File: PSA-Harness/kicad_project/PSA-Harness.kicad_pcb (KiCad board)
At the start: 4 copper layers, 58.3 x 52.5 mm, 20 parts, among them J1 to_EPS_1, J10 B2B_1, J11 B2B_2, J2 to_EPS_2, J3 to_ESP_3, J4 to_car_1, J5 to_car_2, J6 to_car_3, J7 USB_C_Receptacle, J8 B2B_1, J9 B2B_2, U1 DG419LEUA, U2 DG419LEUA

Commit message: cable-board setup
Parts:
- removed J10, J8: B2B_1, Connector_PinHeader_1.27mm:PinHeader_2x15_P1.27mm_Vertical
- removed J11, J9: B2B_2, Connector_PinHeader_1.27mm:PinHeader_2x15_P1.27mm_Vertical
- J4, J5, J6: footprint PSA:ESW-110-44-F-D -> PSA:10129381-920003BLF; moved to F.Cu
- J7: footprint PSA:GCT_USB4115-03-C_REVB4 -> PSA:TYPE-C-31-M-04
- R1, R2, R3, R4: footprint Resistor_SMD:R_0603_1608Metric -> Resistor_SMD:R_1206_3216Metric
- moved J4 60.0 mm to (84.1, 122.2), turned to 90 degrees
- moved J6 60.0 mm to (67.3, 122.2), turned to 90 degrees
- moved J5 60.0 mm to (75.7, 122.2), turned to 90 degrees
- moved J7 11.9 mm to (80.5, 96.4), turned to 180 degrees
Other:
- board outline removed
- board text removed: "PCB1"
- board text removed: "PCB2"

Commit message: components placed
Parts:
- moved J7 49.7 mm to (90.8, 145.0), turned to 0 degrees
- moved D1 47.5 mm to (109.5, 143.5)
- moved D2 47.5 mm to (105.5, 143.5)
- moved D3 47.5 mm to (100.5, 143.5)
- moved U1 47.3 mm to (100.5, 143.3)
- moved U2 47.3 mm to (105.5, 143.3)
- moved R1 47.3 mm to (109.5, 145.0)
- moved R2 47.3 mm to (109.5, 141.6)
- moved R3 47.3 mm to (112.4, 141.6)
- moved R4 47.3 mm to (112.4, 145.0)
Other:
- board outline added: 57 x 41.5 mm

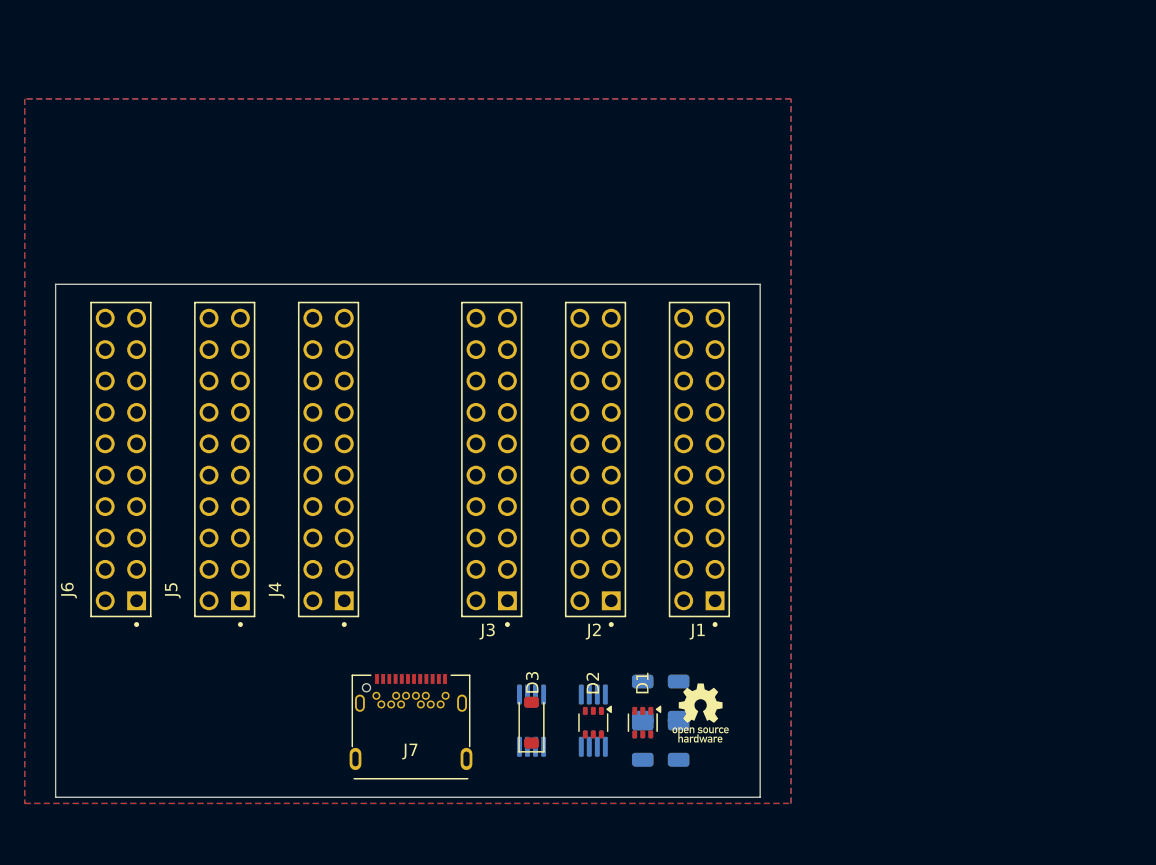
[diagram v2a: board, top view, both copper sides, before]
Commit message: components variant 2
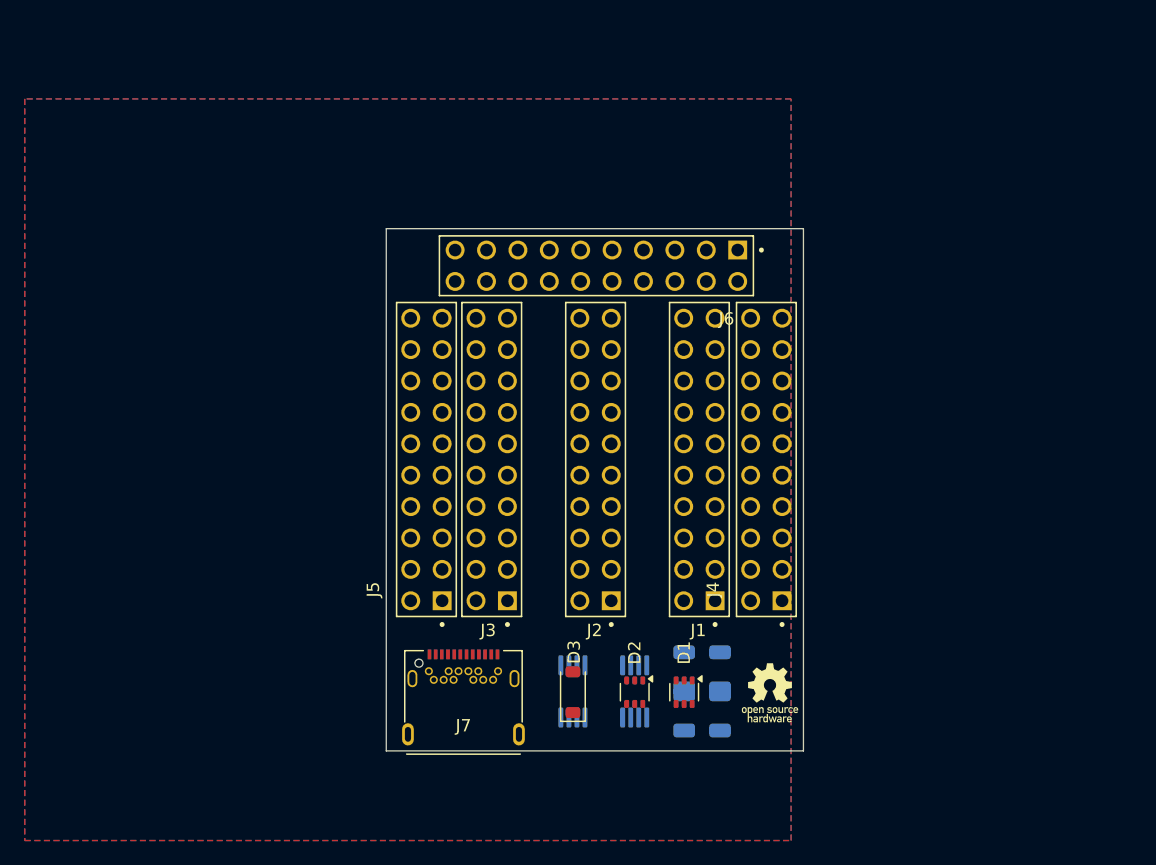
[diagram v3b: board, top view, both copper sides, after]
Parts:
- moved J6 41.5 mm to (105.8, 106.5), turned to 180 degrees
- moved J4 35.4 mm to (119.5, 122.2)
- moved J5 16.3 mm to (92.0, 122.2)
- moved J7 4.69 mm to (95.0, 143.0)
- moved D1 4.16 mm to (112.8, 141.0)
- moved D2 4.16 mm to (108.8, 141.0)
- moved D3 4.16 mm to (103.8, 141.0)
- moved R1 4.10 mm to (112.8, 142.6)
- moved R2 4.10 mm to (112.8, 139.2)
- moved R3 4.10 mm to (115.8, 139.2)
- moved R4 4.10 mm to (115.8, 142.6)
- moved U1 4.10 mm to (103.8, 140.9)
- moved U2 4.10 mm to (108.8, 140.9)
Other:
- board size 57 x 41.5 mm -> 33.8 x 42.2 mm

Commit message: components placed exactly
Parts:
- moved R3 2.48 mm to (118.0, 138.2)
- moved R4 2.38 mm to (118.0, 143.4)
- moved R2 1.31 mm to (113.7, 138.2)
- moved R1 1.11 mm to (113.7, 143.4)
- moved D1 0.78 mm to (113.6, 140.8)
- moved J7 0.55 mm to (95.5, 143.0)
- moved J5 0.22 mm to (91.8, 122.2)
- moved D2 0.20 mm to (108.8, 140.8)
- moved D3 0.20 mm to (103.8, 140.8)
- moved J6 0.14 mm to (105.7, 106.4)
- moved U1 0.14 mm to (103.8, 140.8)
- moved U2 0.14 mm to (108.8, 140.8)
- moved J4 0.08 mm to (119.6, 122.2)
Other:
- board size 33.8 x 42.2 mm -> 33.5 x 43.1 mm

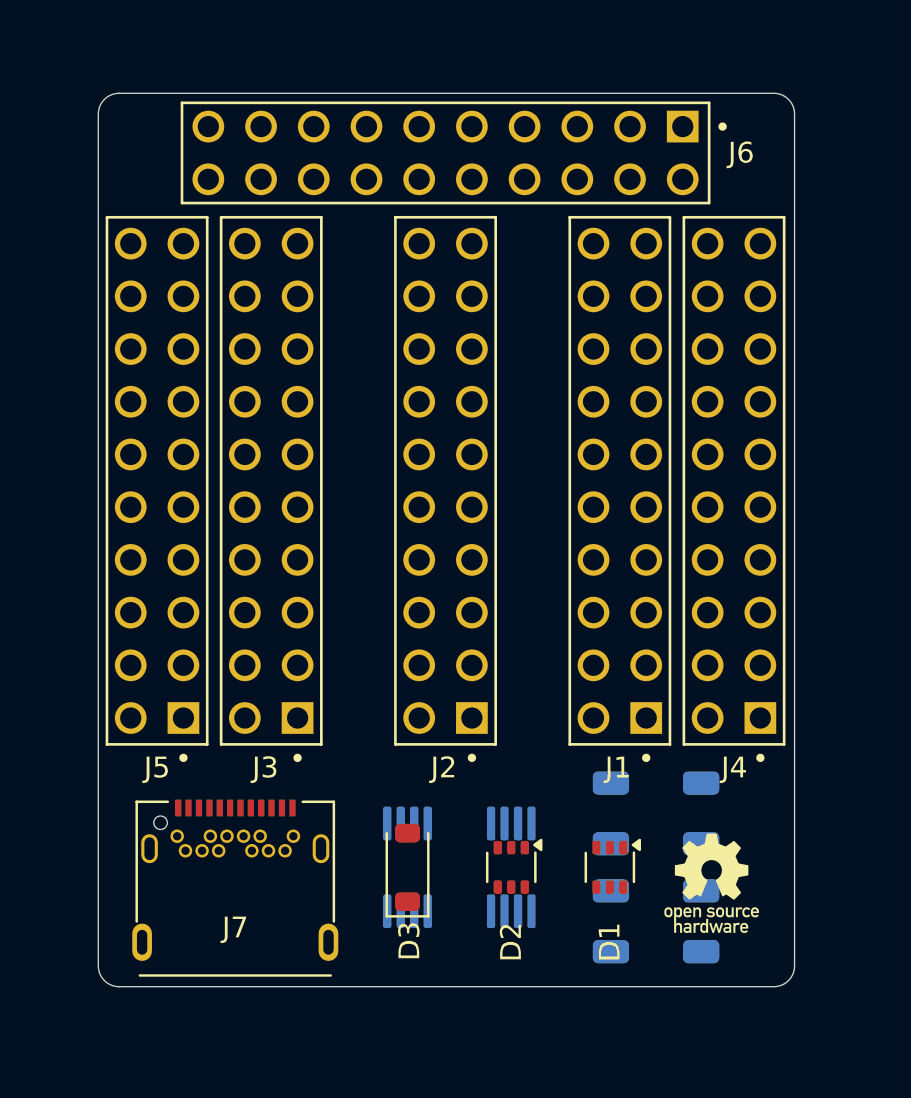
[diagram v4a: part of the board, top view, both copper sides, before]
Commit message: CAN routed
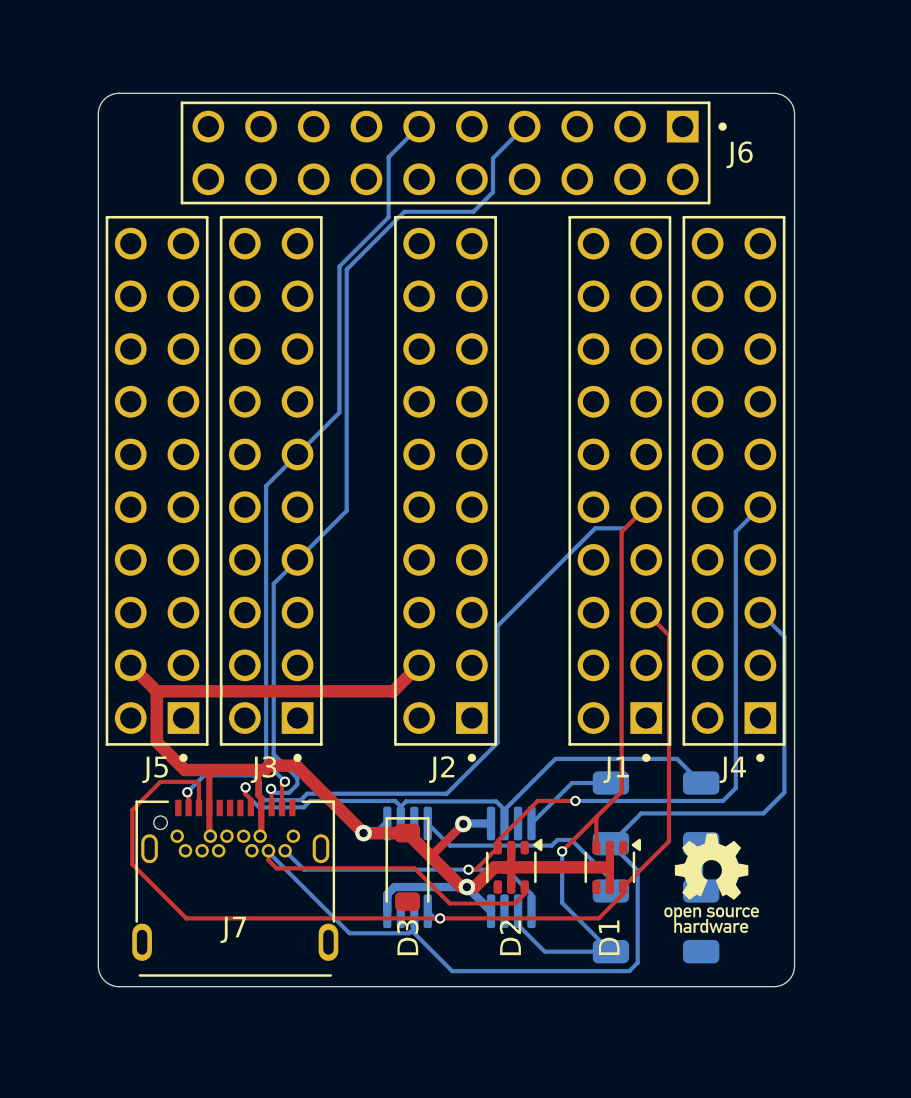
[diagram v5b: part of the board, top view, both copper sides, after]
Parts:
- moved R1 5.20 mm to (113.7, 138.2)
- moved R2 5.20 mm to (113.7, 143.4)
- turned D3 to -90 degrees
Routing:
- net +12V: track 0.00 -> 64.5 mm, vias 0 -> 3
- net CAN0_H: track 0.00 -> 64.5 mm, vias 0 -> 2
- net CAN2_L: track 0.00 -> 61.4 mm
- net CAN0_L: track 0.00 -> 48.5 mm, vias 0 -> 1
- net CAN2_H: track 0.00 -> 42.3 mm, vias 0 -> 2
- net CAN1_L: track 0.00 -> 41.6 mm, vias 0 -> 1
- net CAN1_H: track 0.00 -> 36.3 mm, vias 0 -> 1
- net SBU1: track 0.00 -> 27.9 mm, vias 0 -> 1
- net Net-(R2-Pad1): track 0.00 -> 10.7 mm
- net Net-(R1-Pad2): track 0.00 -> 4.63 mm
- net Net-(R3-Pad2): track 0.00 -> 2.28 mm

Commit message: board routed
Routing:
- net 51: track 0.00 -> 49.8 mm, vias 0 -> 2
- net 41: track 0.00 -> 46.0 mm, vias 0 -> 1
- net 52: track 0.00 -> 43.3 mm, vias 0 -> 1
- net 53: track 0.00 -> 42.7 mm
- net 42: track 0.00 -> 36.0 mm, vias 0 -> 1
- net 43: track 0.00 -> 32.8 mm, vias 0 -> 1
- net 54: track 0.00 -> 29.9 mm, vias 0 -> 1
- net 55: track 0.00 -> 25.6 mm, vias 0 -> 2
- net 45: track 0.00 -> 23.7 mm
- net 56: track 0.00 -> 17.0 mm
- net 36: track 0.00 -> 16.0 mm, vias 0 -> 1
- net 35: track 0.00 -> 14.8 mm
- net 30: track 0.00 -> 14.8 mm
- net 31: track 0.00 -> 14.8 mm
- net 29: track 0.00 -> 14.8 mm
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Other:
- rule pad_to_mask_clearance: 0.038 -> 0

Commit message: move to_car connector to back side
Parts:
- J4, J5, J6: footprint PSA:10129381-920003BLF -> PSA:10129381-920003BLF_BACK; moved to B.Cu
